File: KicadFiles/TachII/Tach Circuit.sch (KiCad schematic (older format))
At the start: 17 parts, among them Q1 2N3904

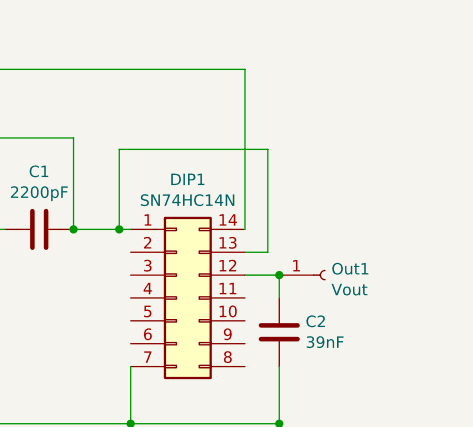
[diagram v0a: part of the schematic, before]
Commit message: Added logo and fixed connectors
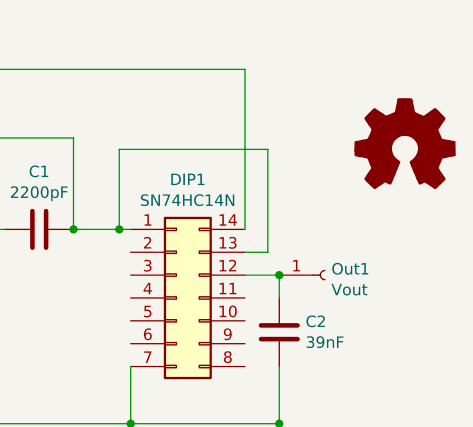
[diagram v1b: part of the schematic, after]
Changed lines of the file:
@@
 Wire Wire Line
 	5250 3300 5250 3550
+$Comp
+L Graphic:Logo_Open_Hardware_Small #LOGO1
+U 1 1 5BE4F1B1
+P 6450 2350
+F 0 "#LOGO1" H 6450 2625 50  0001 C CNN
+F 1 "Logo_Open_Hardware_Small" H 6450 2125 50  0001 C CNN
+F 2 "TestBaja:Baja_Logo_Tach" H 6450 2350 50  0001 C CNN
+F 3 "~" H 6450 2350 50  0001 C CNN
+	1    6450 2350
+	1    0    0    -1
+$EndComp
 $EndSCHEMATC
